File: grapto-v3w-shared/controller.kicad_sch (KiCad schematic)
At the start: 38 parts, among them J1 Conn_01x02_Female, J6 USB_C_Receptacle_USB2.0, J8 Conn_01x06_Male, U1 ACN52840

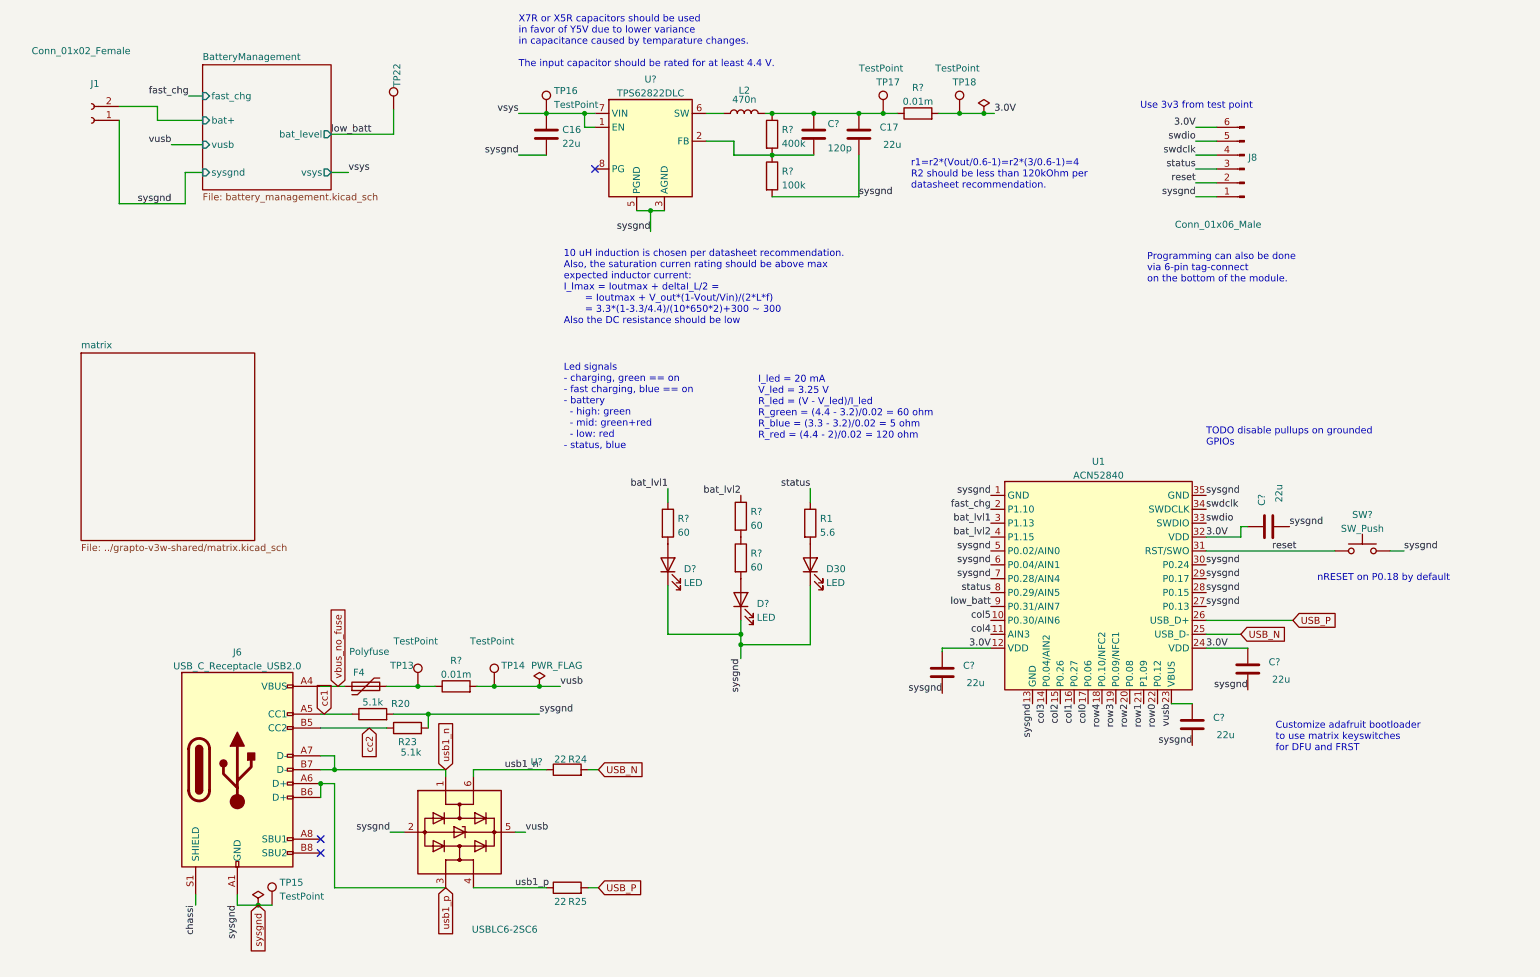
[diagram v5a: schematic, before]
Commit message: Added footprints.
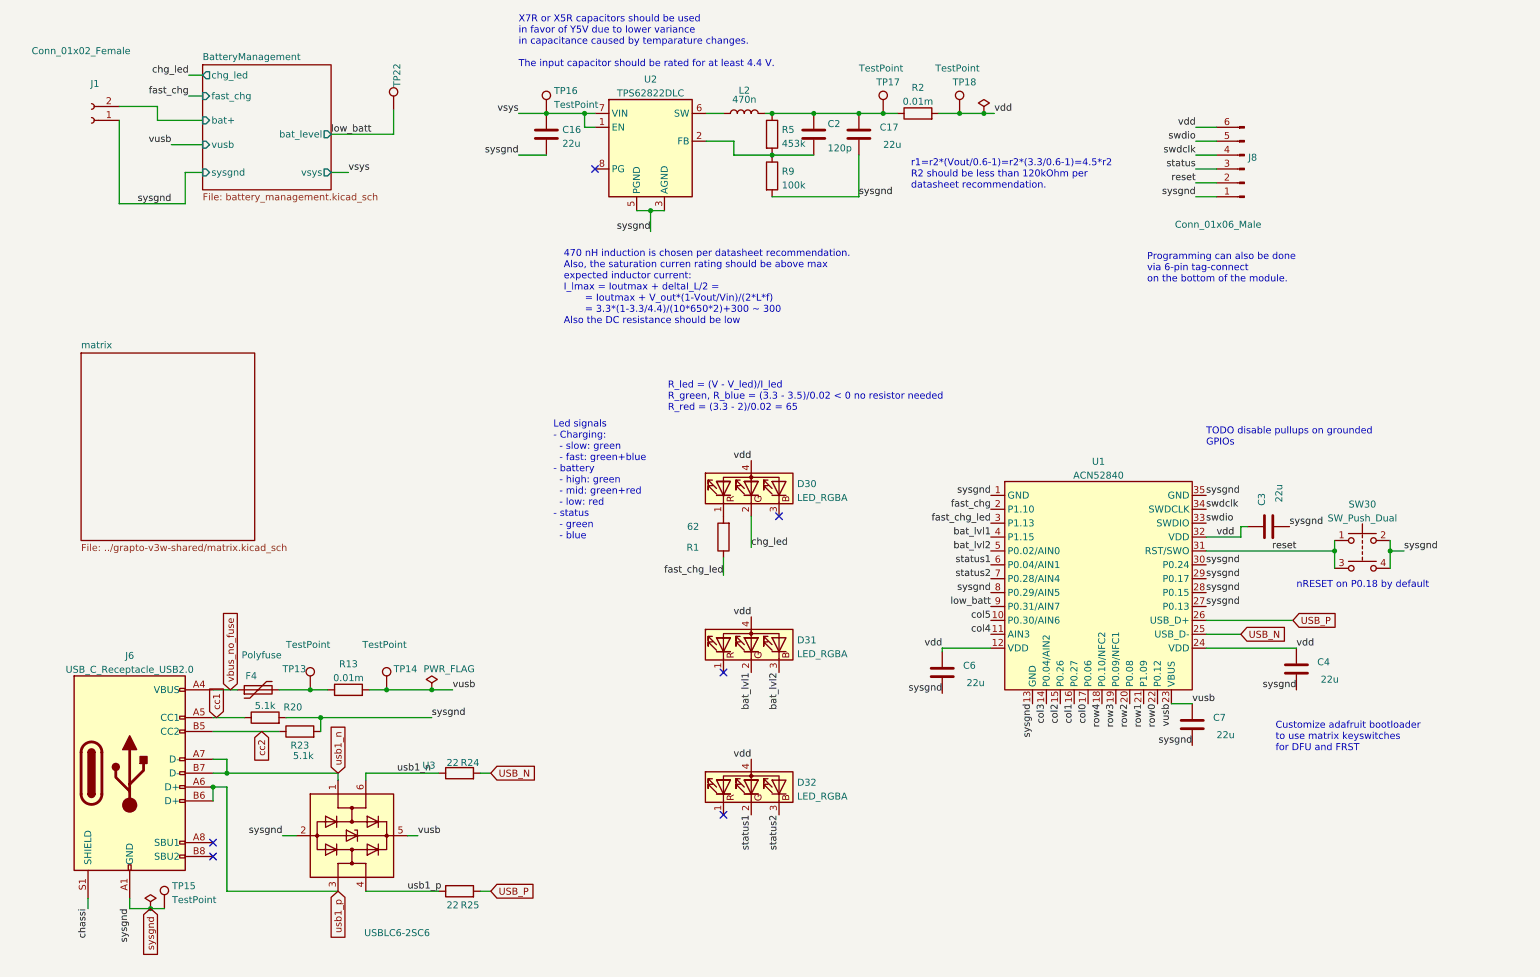
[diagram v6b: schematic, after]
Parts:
- removed D30, D? (x2): LED, LED_SMD:LED_0805_2012Metric_Pad1.15x1.40mm_HandSolder, symbol Device:LED
- removed R? (x3): 60, Resistor_SMD:R_0603_1608Metric_Pad0.98x0.95mm_HandSolder, symbol Device:R
- removed SW?: SW_Push, symbol Switch:SW_Push
- added D30, D31, D32: LED_RGBA, grapto-v3w:LTST-S310F3WT, symbol Device:LED_RGBA
- added SW30: SW_Push_Dual, grapto-v3w:korean k2 1157sp, symbol Switch:SW_Push_Dual
- J6: footprint grapto-v3w:USB_C_Receptacle_molex_2169900001 -> Connector_USB:USB_C_Receptacle_G-Switch_GT-USB-7010ASV
- L2: footprint grapto-v3w:Bourns-SRP0415 -> grapto-v3w:MHCI05020-R47M-R8
- R1: value 5.6 -> 62
- R13, R2, R9: renamed from R?; footprint (none) -> Resistor_SMD:R_0603_1608Metric_Pad0.98x0.95mm_HandSolder
- R5: renamed from R?; value 400k -> 453k; footprint (none) -> Resistor_SMD:R_0603_1608Metric_Pad0.98x0.95mm_HandSolder
- gave numbers to parts that had none: 7
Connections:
- net bat_lvl1: now also U1.4 (P1.15), D31.2 (GK); no longer U1.3 (P1.13)
- net bat_lvl2: now also U1.5 (P0.02/AIN0), D31.3 (BK); no longer U1.4 (P1.15)
- net reset: now also SW30.1, SW30.3
- net status: no longer R1.1, U1.8 (P0.29/AIN5)
- net sysgnd: now also U1.8 (P0.29/AIN5), SW30.2, SW30.4; no longer U1.5 (P0.02/AIN0), U1.6 (P0.04/AIN1), U1.7 (P0.28/AIN4)
- net at R1.2: now also D30.1 (RK)
- net 3.0V renamed vdd
- net vdd: now also D30.4 (A), D31.4 (A), D32.4 (A)
- new net chg_led: D30.2 (GK)
- new net fast_chg_led: R1.1, U1.3 (P1.13)
- new net status1: D32.2 (GK), U1.6 (P0.04/AIN1)
- new net status2: D32.3 (BK), U1.7 (P0.28/AIN4)
- no-connect marks 3 -> 6
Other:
- sheet BatteryManagement ports: added chg_led; removed none
- note added: "470 nH induction is chosen per datasheet recommendation. Also, the saturation curren rating should be above max expected inductor current: I_lmax = Ioutmax + deltaI_L/2 = = Ioutmax + V_out*(1-Vout/Vin)/(2*L*f) = 3.3*(1-3.3/4.4)/(10*650*2)+300 ~ 300 Also the DC resistance should be low"
- note added: "Led signals - Charging: - slow: green - fast: green+blue - battery - high: green - mid: green+red - low: red - status - green - blue"
- note added: "R_led = (V - V_led)/I_led R_green, R_blue = (3.3 - 3.5)/0.02 < 0 no resistor needed R_red = (3.3 - 2)/0.02 = 65"
- note added: "r1=r2*(Vout/0.6-1)=r2*(3.3/0.6-1)=4.5*r2 R2 should be less than 120kOhm per datasheet recommendation."
- note removed: "10 uH induction is chosen per datasheet recommendation. Also, the saturation curren rating should be above max expected inductor current: I_lmax = Ioutmax + deltaI_L/2 = = Ioutmax + V_out*(1-Vout/Vin)/(2*L*f) = 3.3*(1-3.3/4.4)/(10*650*2)+300 ~ 300 Also the DC resistance should be low"
- note removed: "I_led = 20 mA V_led = 3.25 V R_led = (V - V_led)/I_led R_green = (4.4 - 3.2)/0.02 = 60 ohm R_blue = (3.3 - 3.2)/0.02 = 5 ohm R_red = (4.4 - 2)/0.02 = 120 ohm"
- note removed: "Led signals - charging, green == on - fast charging, blue == on - battery - high: green - mid: green+red - low: red - status, blue"
- note removed: "Use 3v3 from test point"
- note removed: "r1=r2*(Vout/0.6-1)=r2*(3/0.6-1)=4 R2 should be less than 120kOhm per datasheet recommendation."
- moved on the sheet: C4, F4, J6, R13, R20, R23, R24, R25, TP13, TP14, TP15, U3

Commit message: before adding hotswaps
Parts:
- removed D30, D31, D32: LED_RGBA, grapto-v3w:LTST-S310F3WT, symbol Device:LED_RGBA
- added D30, D31, D32: LED_ARGB, grapto-v3w:23-23B-R6GHBHC-A01-2A, symbol Device:LED_ARGB
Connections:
- net bat_lvl1: now also D31.3 (GK)
- net bat_lvl2: now also D31.4 (BK)
- net chg_led: now also D30.3 (GK)
- net status1: now also D32.3 (GK)
- net status2: now also D32.4 (BK)
- net vdd: now also D30.1 (A), D31.1 (A), D32.1 (A)
- net at R1.2: now also D30.2 (RK)
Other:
- note added: "R_led = (V - V_led)/I_led R_green, R_blue = (3.3 - 3.3)/0.02 = 0 no resistor needed R_red = (3.3 - 2)/0.02 = 65"
- note removed: "R_led = (V - V_led)/I_led R_green, R_blue = (3.3 - 3.5)/0.02 < 0 no resistor needed R_red = (3.3 - 2)/0.02 = 65"
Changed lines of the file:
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@@
     (effects (font (size 1.27 1.27)) (justify left bottom))
   )
-  (text "R_led = (V - V_led)/I_led\nR_green, R_blue = (3.3 - 3.5)/0.02 < 0 no resistor needed\nR_red = (3.3 - 2)/0.02 = 65"
+  (text "R_led = (V - V_led)/I_led\nR_green, R_blue = (3.3 - 3.3)/0.02 = 0 no resistor needed\nR_red = (3.3 - 2)/0.02 = 65"
     (at 138.43 88.9 0)
     (effects (font (size 1.27 1.27)) (justify left bottom))
@@
     (pin "2")
   )
+  (symbol (lib_id "Device:LED_ARGB") (at 153.67 102.87 90) (unit 1)
+    (in_bom yes) (on_board yes) (fields_autoplaced)
+    (property "Reference" "D30" (id 0) (at 162.052 102.0353 90)
+      (effects (font (size 1.27 1.27)) (justify right))
+    )
+    (property "Value" "LED_ARGB" (id 1) (at 162.052 104.5722 90)
+      (effects (font (size 1.27 1.27)) (justify right))
+    )
+    (property "Footprint" "grapto-v3w:23-23B-R6GHBHC-A01-2A" (id 2) (at 154.94 102.87 0)
+      (effects (font (size 1.27 1.27)) hide)
+    )
+    (property "Datasheet" "~" (id 3) (at 154.94 102.87 0)
+      (effects (font (size 1.27 1.27)) hide)
+    )
+    (pin "1")
+    (pin "2")
+    (pin "3")
+    (pin "4")
+  )
   (symbol (lib_id "Connector:TestPoint") (at 88.265 33.655 0) (unit 1)
     (in_bom yes) (on_board yes)
@@
     (pin "6")
   )
-  (symbol (lib_id "Device:LED_RGBA") (at 153.67 157.48 90) (unit 1)
-    (in_bom yes) (on_board yes) (fields_autoplaced)
-    (property "Reference" "D32" (id 0) (at 162.052 156.6453 90)
-      (effects (font (size 1.27 1.27)) (justify right))
-    )
-    (property "Value" "LED_RGBA" (id 1) (at 162.052 159.1822 90)
-      (effects (font (size 1.27 1.27)) (justify right))
-    )
-    (property "Footprint" "grapto-v3w:LTST-S310F3WT" (id 2) (at 154.94 157.48 0)
-      (effects (font (size 1.27 1.27)) hide)
-    )
-    (property "Datasheet" "~" (id 3) (at 154.94 157.48 0)
-      (effects (font (size 1.27 1.27)) hide)
-    )
-    (pin "1")
-    (pin "2")
-    (pin "3")
-    (pin "4")
-  )
   (symbol (lib_id "Connector:Conn_01x02_Female") (at 33.02 35.56 180) (unit 1)
     (in_bom yes) (on_board yes)
@@
     (pin "2")
   )
-  (symbol (lib_id "Connector:TestPoint") (at 46.355 179.705 0) (unit 1)
-    (in_bom yes) (on_board yes) (fields_autoplaced)
-    (property "Reference" "TP15" (id 0) (at 47.752 175.5683 0)
-      (effects (font (size 1.27 1.27)) (justify left))
-    )
-    (property "Value" "TestPoint" (id 1) (at 47.752 178.1052 0)
-      (effects (font (size 1.27 1.27)) (justify left))
-    )
-    (property "Footprint" "grapto-v3w:TestPoint_THTPad_D2.0mm_Drill1.0mm" (id 2) (at 51.435 179.705 0)
-      (effects (font (size 1.27 1.27)) hide)
-    )
-    (property "Datasheet" "~" (id 3) (at 51.435 179.705 0)
-      (effects (font (size 1.27 1.27)) hide)
-    )
-    (pin "1")
-  )
-  (symbol (lib_id "Device:LED_RGBA") (at 153.67 131.445 90) (unit 1)
+  (symbol (lib_id "Device:LED_ARGB") (at 153.67 131.445 90) (unit 1)
     (in_bom yes) (on_board yes) (fields_autoplaced)
     (property "Reference" "D31" (id 0) (at 162.052 130.6103 90)
       (effects (font (size 1.27 1.27)) (justify right))
     )
-    (property "Value" "LED_RGBA" (id 1) (at 162.052 133.1472 90)
+    (property "Value" "LED_ARGB" (id 1) (at 162.052 133.1472 90)
       (effects (font (size 1.27 1.27)) (justify right))
     )
-    (property "Footprint" "grapto-v3w:LTST-S310F3WT" (id 2) (at 154.94 131.445 0)
+    (property "Footprint" "grapto-v3w:23-23B-R6GHBHC-A01-2A" (id 2) (at 154.94 131.445 0)
       (effects (font (size 1.27 1.27)) hide)
     )
@@
     (pin "3")
     (pin "4")
+  )
+  (symbol (lib_id "Connector:TestPoint") (at 46.355 179.705 0) (unit 1)
+    (in_bom yes) (on_board yes) (fields_autoplaced)
+    (property "Reference" "TP15" (id 0) (at 47.752 175.5683 0)
+      (effects (font (size 1.27 1.27)) (justify left))
+    )
+    (property "Value" "TestPoint" (id 1) (at 47.752 178.1052 0)
+      (effects (font (size 1.27 1.27)) (justify left))
+    )
+    (property "Footprint" "grapto-v3w:TestPoint_THTPad_D2.0mm_Drill1.0mm" (id 2) (at 51.435 179.705 0)
+      (effects (font (size 1.27 1.27)) hide)
+    )
+    (property "Datasheet" "~" (id 3) (at 51.435 179.705 0)
+      (effects (font (size 1.27 1.27)) hide)
+    )
+    (pin "1")
   )
   (symbol (lib_id "Device:R") (at 71.12 147.32 90) (unit 1)
@@
     (pin "7")
     (pin "8")
+  )
+  (symbol (lib_id "Device:LED_ARGB") (at 153.67 157.48 90) (unit 1)
+    (in_bom yes) (on_board yes) (fields_autoplaced)
+    (property "Reference" "D32" (id 0) (at 162.052 156.6453 90)
+      (effects (font (size 1.27 1.27)) (justify right))
+    )
+    (property "Value" "LED_ARGB" (id 1) (at 162.052 159.1822 90)
+      (effects (font (size 1.27 1.27)) (justify right))
+    )
+    (property "Footprint" "grapto-v3w:23-23B-R6GHBHC-A01-2A" (id 2) (at 154.94 157.48 0)
+      (effects (font (size 1.27 1.27)) hide)
+    )
+    (property "Datasheet" "~" (id 3) (at 154.94 157.48 0)
+      (effects (font (size 1.27 1.27)) hide)
+    )
+    (pin "1")
+    (pin "2")
+    (pin "3")
+    (pin "4")
   )
   (symbol (lib_id "Device:R") (at 80.01 139.7 90) (unit 1)
@@
     (pin "2")
   )
-  (symbol (lib_id "Device:LED_RGBA") (at 153.67 102.87 90) (unit 1)
-    (in_bom yes) (on_board yes) (fields_autoplaced)
-    (property "Reference" "D30" (id 0) (at 162.052 102.0353 90)
-      (effects (font (size 1.27 1.27)) (justify right))
-    )
-    (property "Value" "LED_RGBA" (id 1) (at 162.052 104.5722 90)
-      (effects (font (size 1.27 1.27)) (justify right))
-    )
-    (property "Footprint" "grapto-v3w:LTST-S310F3WT" (id 2) (at 154.94 102.87 0)
-      (effects (font (size 1.27 1.27)) hide)
-    )
-    (property "Datasheet" "~" (id 3) (at 154.94 102.87 0)
-      (effects (font (size 1.27 1.27)) hide)
-    )
-    (pin "1")
-    (pin "2")
-    (pin "3")
-    (pin "4")
-  )
   (symbol (lib_id "Device:R") (at 184.15 34.29 90) (unit 1)

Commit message: left half pcb draft.
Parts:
- removed SW30: SW_Push_Dual, grapto-v3w:korean k2 1157sp, symbol Switch:SW_Push_Dual
- added J2: Conn_01x01_Female, symbol Connector:Conn_01x01_Female
- TP13, TP14, TP15, TP16, TP17, TP18, TP22: footprint grapto-v3w:TestPoint_THTPad_D2.0mm_Drill1.0mm -> Connector_PinHeader_2.54mm:PinHeader_1x01_P2.54mm_Vertical
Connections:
- net status is gone; now on net status1: J8.3 (Pin_3)
- net chassi: now also J2.1 (Pin_1)
- net usb1_n: no longer R24.1, U3.6 (I/O1)
- net usb1_p: no longer R25.1, U3.4 (I/O2)
- new net USB0_N: R24.1, U3.6 (I/O1)
- new net USB0_P: R25.1, U3.4 (I/O2)
